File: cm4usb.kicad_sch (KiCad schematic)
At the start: 24 parts, among them J6 USB4110-GF-A, J7 USB4110-GF-A, U11 USB3740B-AI2, U12 AP22653FDZ-7

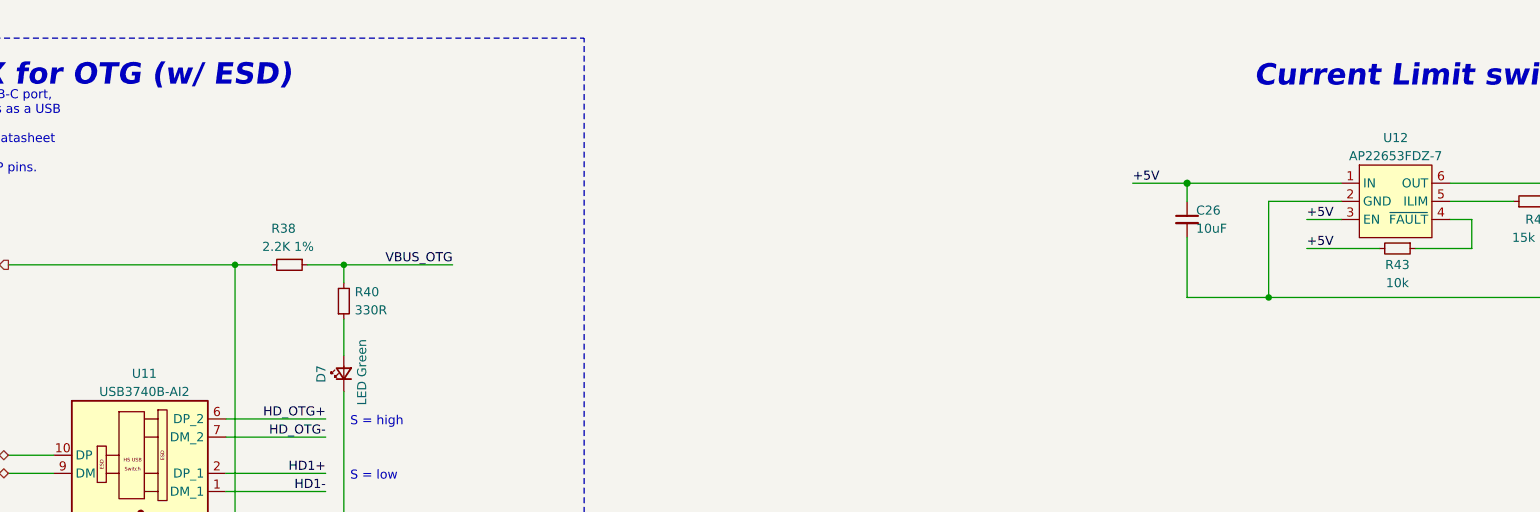
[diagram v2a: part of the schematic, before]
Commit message: added ti buffer lib
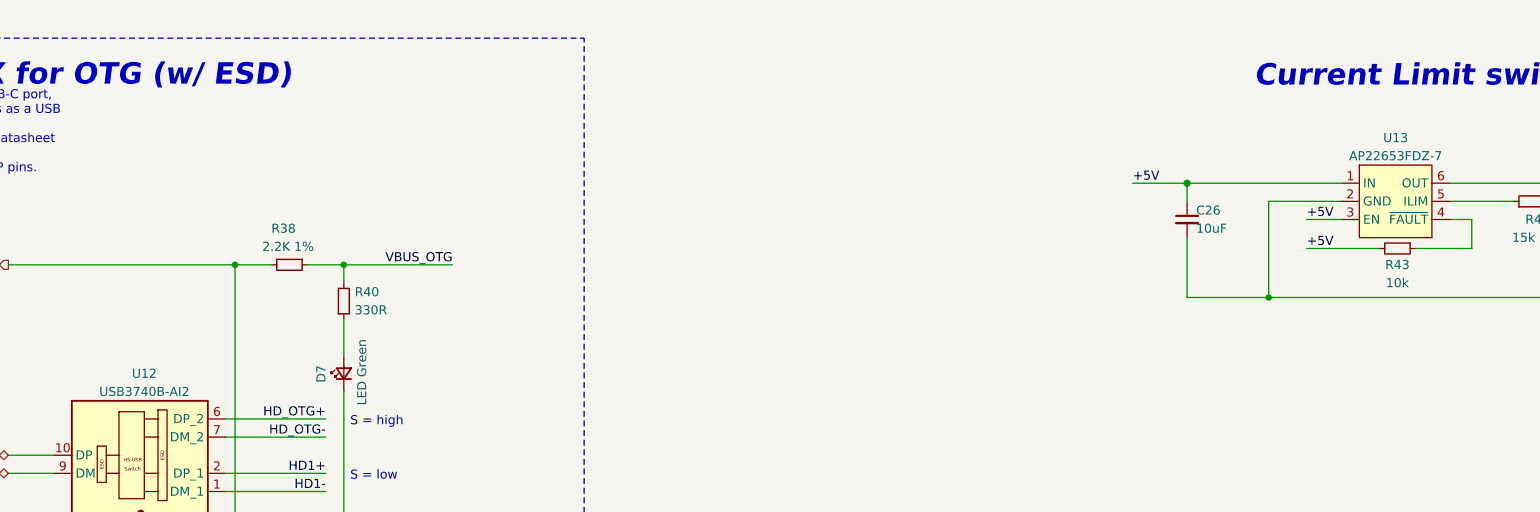
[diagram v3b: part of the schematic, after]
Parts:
- renumbered U11 to U12, U12 to U13
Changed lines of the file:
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@@
   (symbol (lib_id "power:GND") (at 368.3 94.742 0) (unit 1)
     (in_bom yes) (on_board yes)
-    (property "Reference" "#PWR039" (id 0) (at 368.3 101.092 0)
+    (property "Reference" "#PWR041" (id 0) (at 368.3 101.092 0)
       (effects (font (size 1.27 1.27)) hide)
     )
@@
   (symbol (lib_id "power:GND") (at 106.68 151.13 0) (unit 1)
     (in_bom yes) (on_board yes)
-    (property "Reference" "#PWR036" (id 0) (at 106.68 157.48 0)
+    (property "Reference" "#PWR038" (id 0) (at 106.68 157.48 0)
       (effects (font (size 1.27 1.27)) hide)
     )
@@
   (symbol (lib_id "power:GND") (at 95.25 262.89 0) (unit 1)
     (in_bom yes) (on_board yes)
-    (property "Reference" "#PWR035" (id 0) (at 95.25 269.24 0)
+    (property "Reference" "#PWR037" (id 0) (at 95.25 269.24 0)
       (effects (font (size 1.27 1.27)) hide)
     )
@@
   (symbol (lib_id "power:GND") (at 149.86 151.13 0) (unit 1)
     (in_bom yes) (on_board yes)
-    (property "Reference" "#PWR037" (id 0) (at 149.86 157.48 0)
+    (property "Reference" "#PWR039" (id 0) (at 149.86 157.48 0)
       (effects (font (size 1.27 1.27)) hide)
     )
@@
   (symbol (lib_id "Power_Protection_Diodes:AP22653FDZ-7") (at 297.18 78.74 0) (unit 1)
     (in_bom yes) (on_board yes)
-    (property "Reference" "U12" (id 0) (at 297.18 69.85 0))
+    (property "Reference" "U13" (id 0) (at 297.18 69.85 0))
     (property "Value" "AP22653FDZ-7" (id 1) (at 297.18 72.39 0))
     (property "Footprint" "Power_Protection_Diodes:Diodes_W-DFN2020-6_A1" (id 2) (at 297.18 92.71 0)
@@
   (symbol (lib_id "Interface_USB_Microchip:USB3740B-AI2") (at 121.285 116.84 0) (unit 1)
     (in_bom yes) (on_board yes)
-    (property "Reference" "U11" (id 0) (at 121.92 102.87 0))
+    (property "Reference" "U12" (id 0) (at 121.92 102.87 0))
     (property "Value" "USB3740B-AI2" (id 1) (at 121.92 105.41 0))
     (property "Footprint" "Interface_USB_Microchip:Microchip_UQFN-10_1.3x1.8mm_P0.4mm_pin1" (id 2) (at 121.285 149.86 0)
@@
   (symbol (lib_id "power:GND") (at 219.71 262.89 0) (unit 1)
     (in_bom yes) (on_board yes)
-    (property "Reference" "#PWR038" (id 0) (at 219.71 269.24 0)
+    (property "Reference" "#PWR040" (id 0) (at 219.71 269.24 0)
       (effects (font (size 1.27 1.27)) hide)
     )
@@
   (symbol (lib_id "power:GND") (at 85.09 138.43 0) (mirror y) (unit 1)
     (in_bom yes) (on_board yes)
-    (property "Reference" "#PWR034" (id 0) (at 85.09 144.78 0)
-      (effects (font (size 1.27 1.27)) hide)
-    )
+    (property "Reference" "#PWR036" (id 0) (at 85.09 144.78 0)
+      (effects (font (size 1.27 1.27)) hide)
+    )

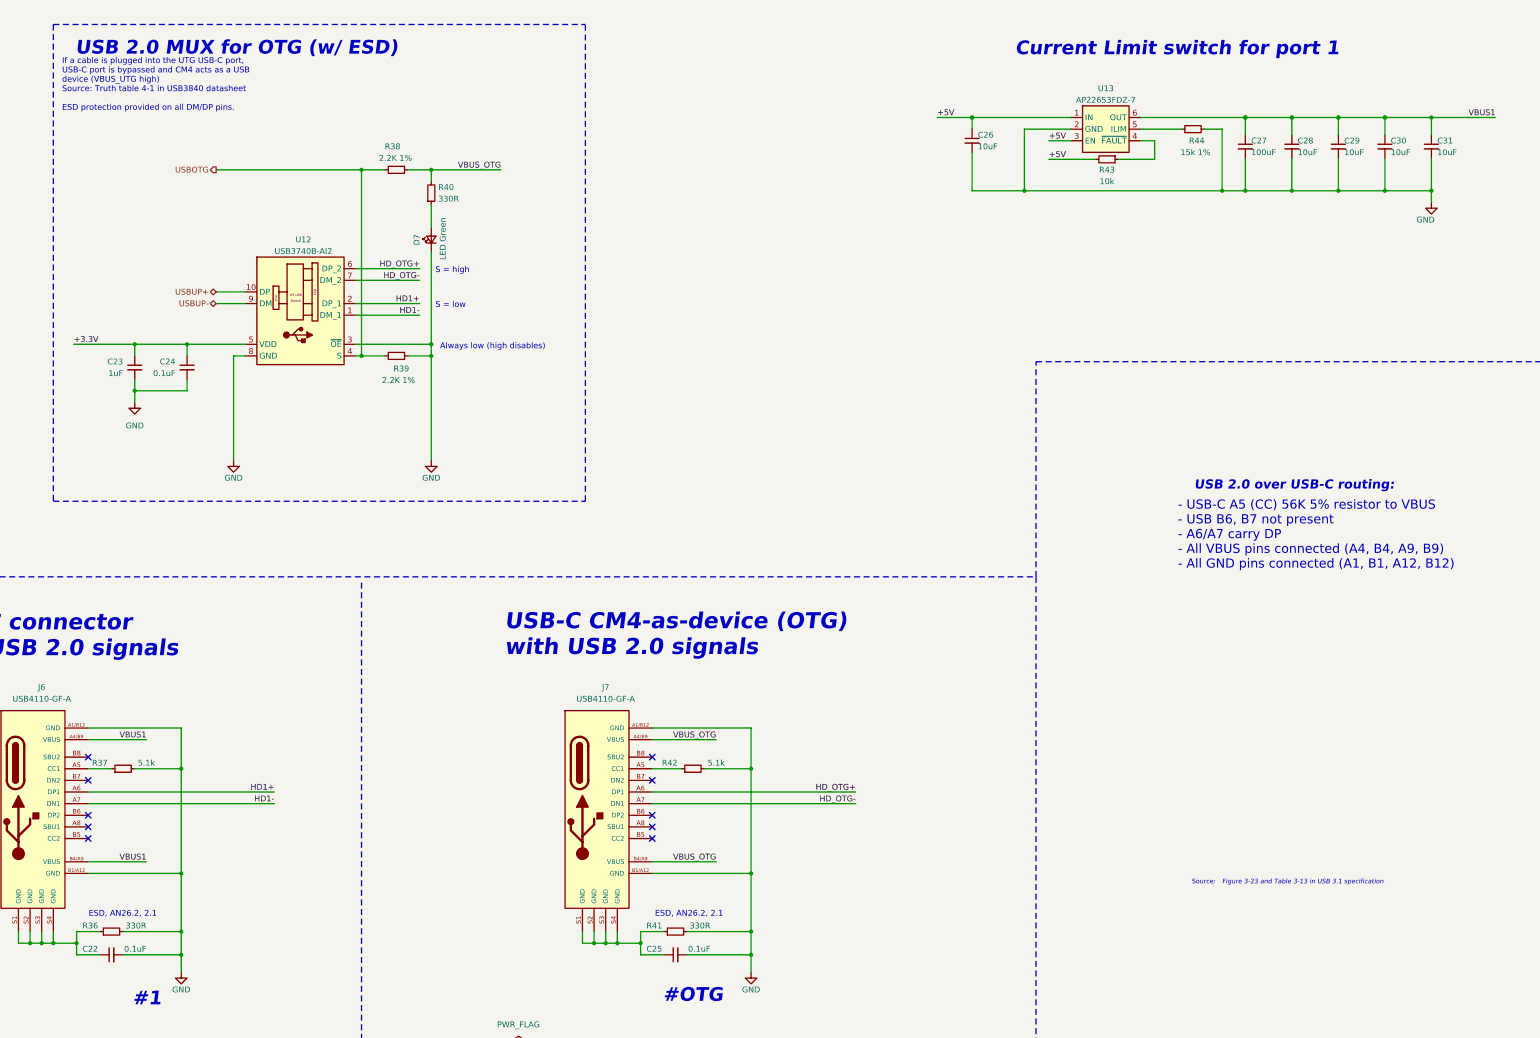
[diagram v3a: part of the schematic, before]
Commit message: initial integration of i2c arbiter
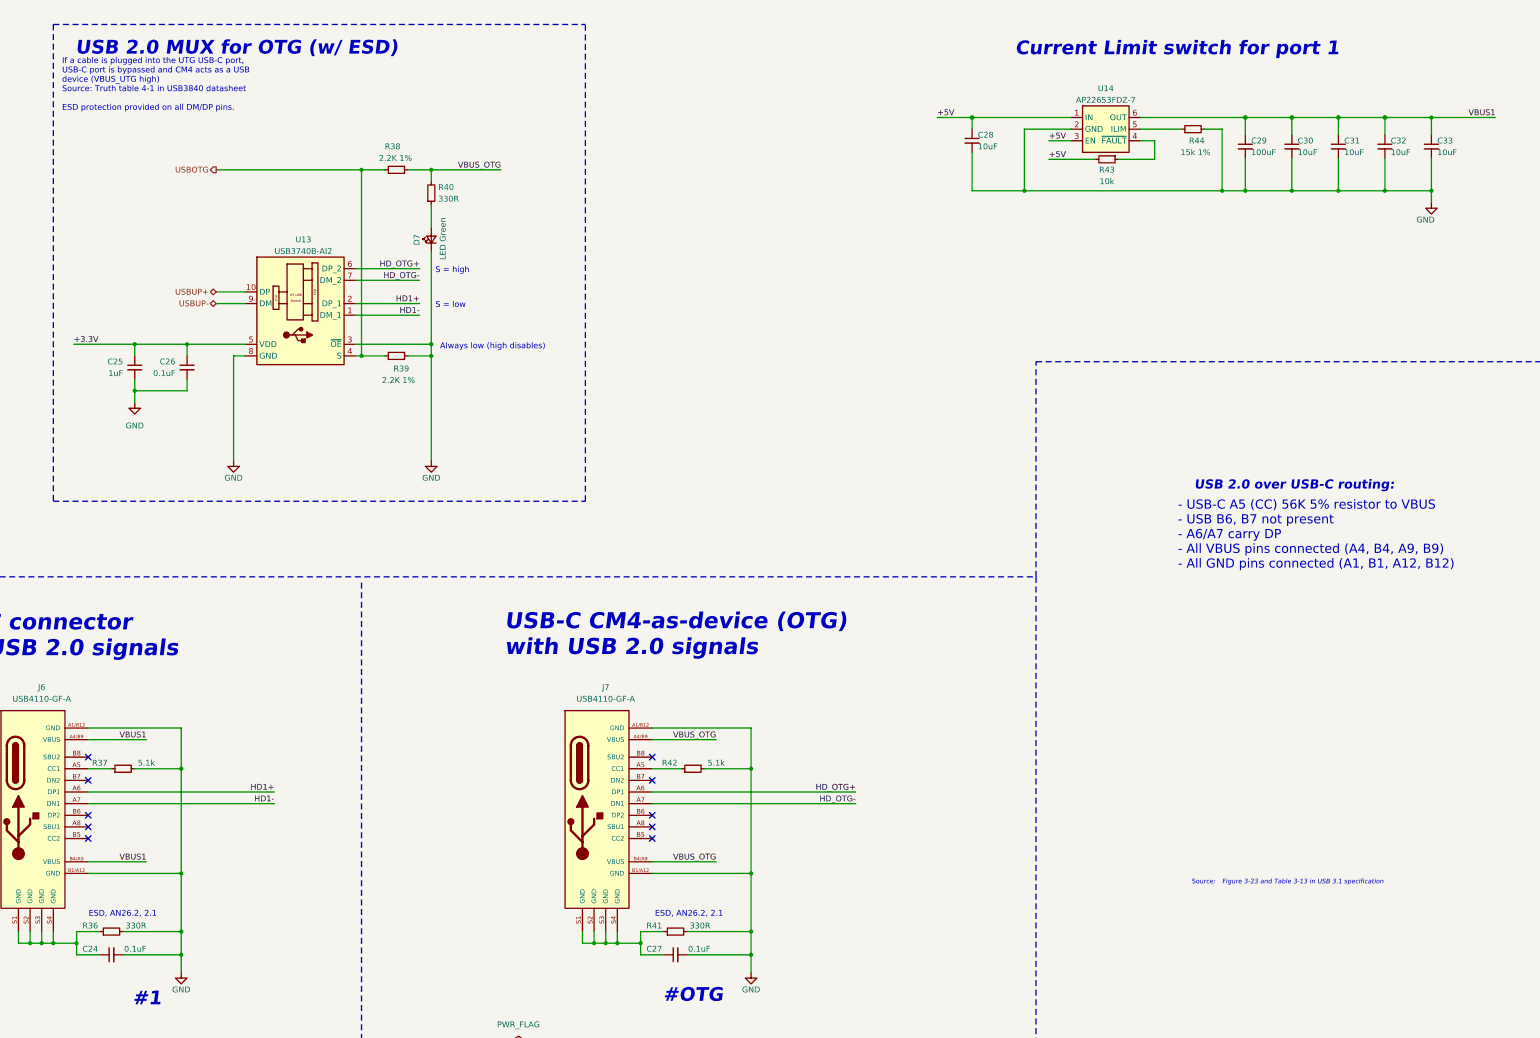
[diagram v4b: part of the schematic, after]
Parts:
- renumbered C22 to C24, C23 to C25, C24 to C26, C25 to C27, C26 to C28, C27 to C29, C28 to C30, C29 to C31, C30 to C32, C31 to C33, U12 to U13, U13 to U14
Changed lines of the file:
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@@
   (symbol (lib_id "Device:C_Small") (at 337.82 82.55 0) (unit 1)
     (in_bom yes) (on_board yes)
-    (property "Reference" "C28" (id 0) (at 339.09 81.28 0)
+    (property "Reference" "C30" (id 0) (at 339.09 81.28 0)
       (effects (font (size 1.27 1.27)) (justify left))
     )
@@
   (symbol (lib_id "Device:C_Small") (at 327.66 82.55 0) (unit 1)
     (in_bom yes) (on_board yes)
-    (property "Reference" "C27" (id 0) (at 328.93 81.28 0)
+    (property "Reference" "C29" (id 0) (at 328.93 81.28 0)
       (effects (font (size 1.27 1.27)) (justify left))
     )
@@
   (symbol (lib_id "power:GND") (at 368.3 94.742 0) (unit 1)
     (in_bom yes) (on_board yes)
-    (property "Reference" "#PWR041" (id 0) (at 368.3 101.092 0)
+    (property "Reference" "#PWR042" (id 0) (at 368.3 101.092 0)
       (effects (font (size 1.27 1.27)) hide)
     )
@@
   (symbol (lib_id "Device:C_Small") (at 347.98 82.55 0) (unit 1)
     (in_bom yes) (on_board yes)
-    (property "Reference" "C29" (id 0) (at 349.25 81.28 0)
+    (property "Reference" "C31" (id 0) (at 349.25 81.28 0)
       (effects (font (size 1.27 1.27)) (justify left))
     )
@@
   (symbol (lib_id "Device:C_Small") (at 358.14 82.55 0) (unit 1)
     (in_bom yes) (on_board yes)
-    (property "Reference" "C30" (id 0) (at 359.41 81.28 0)
+    (property "Reference" "C32" (id 0) (at 359.41 81.28 0)
       (effects (font (size 1.27 1.27)) (justify left))
     )
@@
   (symbol (lib_id "Device:C_Small") (at 203.2 259.08 90) (unit 1)
     (in_bom yes) (on_board yes)
-    (property "Reference" "C25" (id 0) (at 196.85 257.81 90)
+    (property "Reference" "C27" (id 0) (at 196.85 257.81 90)
       (effects (font (size 1.27 1.27)) (justify right))
     )
@@
   (symbol (lib_id "Device:C_Small") (at 368.3 82.55 0) (unit 1)
     (in_bom yes) (on_board yes)
-    (property "Reference" "C31" (id 0) (at 369.57 81.28 0)
+    (property "Reference" "C33" (id 0) (at 369.57 81.28 0)
       (effects (font (size 1.27 1.27)) (justify left))
     )
@@
   (symbol (lib_id "power:GND") (at 106.68 151.13 0) (unit 1)
     (in_bom yes) (on_board yes)
-    (property "Reference" "#PWR038" (id 0) (at 106.68 157.48 0)
+    (property "Reference" "#PWR039" (id 0) (at 106.68 157.48 0)
       (effects (font (size 1.27 1.27)) hide)
     )
@@
   (symbol (lib_id "power:GND") (at 95.25 262.89 0) (unit 1)
     (in_bom yes) (on_board yes)
-    (property "Reference" "#PWR037" (id 0) (at 95.25 269.24 0)
+    (property "Reference" "#PWR038" (id 0) (at 95.25 269.24 0)
       (effects (font (size 1.27 1.27)) hide)
     )
@@
   (symbol (lib_id "power:GND") (at 149.86 151.13 0) (unit 1)
     (in_bom yes) (on_board yes)
-    (property "Reference" "#PWR039" (id 0) (at 149.86 157.48 0)
+    (property "Reference" "#PWR040" (id 0) (at 149.86 157.48 0)
       (effects (font (size 1.27 1.27)) hide)
     )
@@
   (symbol (lib_id "Power_Protection_Diodes:AP22653FDZ-7") (at 297.18 78.74 0) (unit 1)
     (in_bom yes) (on_board yes)
-    (property "Reference" "U13" (id 0) (at 297.18 69.85 0))
+    (property "Reference" "U14" (id 0) (at 297.18 69.85 0))
     (property "Value" "AP22653FDZ-7" (id 1) (at 297.18 72.39 0))
     (property "Footprint" "Power_Protection_Diodes:Diodes_W-DFN2020-6_A1" (id 2) (at 297.18 92.71 0)
@@
   (symbol (lib_id "Interface_USB_Microchip:USB3740B-AI2") (at 121.285 116.84 0) (unit 1)
     (in_bom yes) (on_board yes)
-    (property "Reference" "U12" (id 0) (at 121.92 102.87 0))
+    (property "Reference" "U13" (id 0) (at 121.92 102.87 0))
     (property "Value" "USB3740B-AI2" (id 1) (at 121.92 105.41 0))
     (property "Footprint" "Interface_USB_Microchip:Microchip_UQFN-10_1.3x1.8mm_P0.4mm_pin1" (id 2) (at 121.285 149.86 0)
@@
   (symbol (lib_id "Device:C_Small") (at 80.01 259.08 90) (unit 1)
     (in_bom yes) (on_board yes)
-    (property "Reference" "C22" (id 0) (at 73.66 257.81 90)
+    (property "Reference" "C24" (id 0) (at 73.66 257.81 90)
       (effects (font (size 1.27 1.27)) (justify right))
     )
@@
   (symbol (lib_id "Device:C_Small") (at 85.09 130.81 0) (mirror y) (unit 1)
     (in_bom yes) (on_board yes) (fields_autoplaced)
-    (property "Reference" "C23" (id 0) (at 82.55 129.54 0)
+    (property "Reference" "C25" (id 0) (at 82.55 129.54 0)
       (effects (font (size 1.27 1.27)) (justify left))
     )
@@
   (symbol (lib_id "power:GND") (at 219.71 262.89 0) (unit 1)
     (in_bom yes) (on_board yes)
-    (property "Reference" "#PWR040" (id 0) (at 219.71 269.24 0)
+    (property "Reference" "#PWR041" (id 0) (at 219.71 269.24 0)
       (effects (font (size 1.27 1.27)) hide)
     )
@@
   (symbol (lib_id "Device:C_Small") (at 267.97 81.28 0) (unit 1)
     (in_bom yes) (on_board yes)
-    (property "Reference" "C26" (id 0) (at 269.24 80.01 0)
+    (property "Reference" "C28" (id 0) (at 269.24 80.01 0)
       (effects (font (size 1.27 1.27)) (justify left))
     )
@@
   (symbol (lib_id "Device:C_Small") (at 96.52 130.81 0) (mirror y) (unit 1)
     (in_bom yes) (on_board yes) (fields_autoplaced)
-    (property "Reference" "C24" (id 0) (at 93.98 129.54 0)
+    (property "Reference" "C26" (id 0) (at 93.98 129.54 0)
       (effects (font (size 1.27 1.27)) (justify left))
     )
@@
   (symbol (lib_id "power:GND") (at 85.09 138.43 0) (mirror y) (unit 1)
     (in_bom yes) (on_board yes)
-    (property "Reference" "#PWR036" (id 0) (at 85.09 144.78 0)
-      (effects (font (size 1.27 1.27)) hide)
-    )
+    (property "Reference" "#PWR037" (id 0) (at 85.09 144.78 0)
+      (effects (font (size 1.27 1.27)) hide)
+    )
